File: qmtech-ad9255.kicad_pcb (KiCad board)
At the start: 4 copper layers, 50 x 80 mm, 49 parts

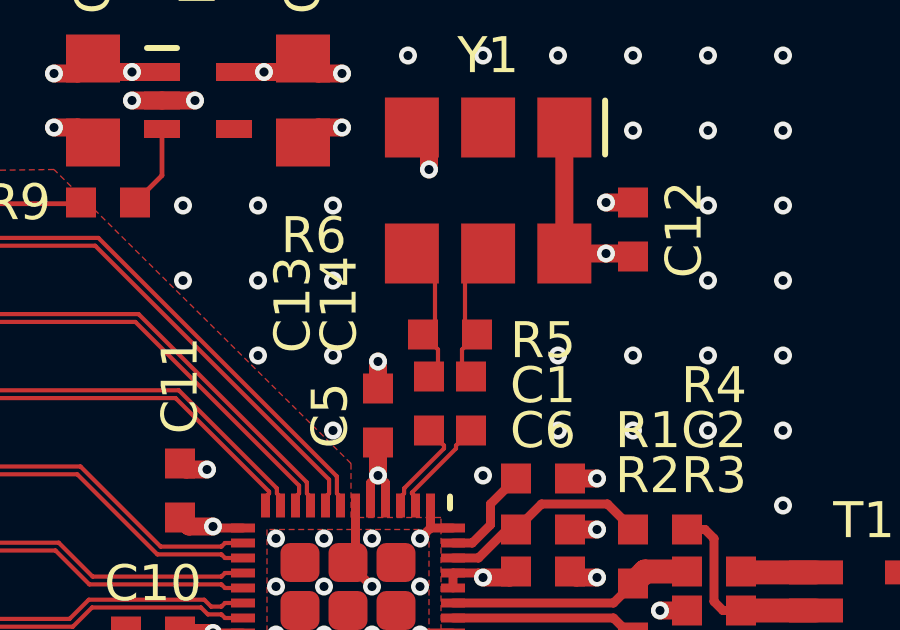
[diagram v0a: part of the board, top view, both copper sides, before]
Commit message: set width of clock traces to 0.3 in qmtech-ad9255
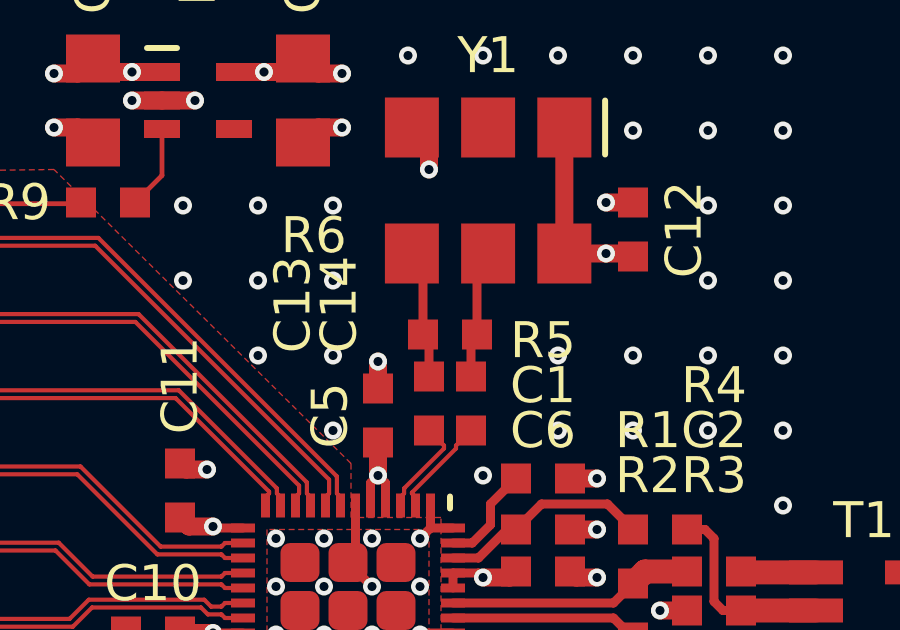
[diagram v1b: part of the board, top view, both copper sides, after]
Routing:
- net CLK-: track 4.92 -> 4.34 mm
- net CLK+: track 4.92 -> 4.34 mm
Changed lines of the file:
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@@
   (segment (start 150.2 97.17) (end 150.2 97.45) (width 0.14) (layer "F.Cu") (net 38))
   (segment (start 150.2 97.45) (end 150.25 97.5) (width 0.14) (layer "F.Cu") (net 38))
-  (segment (start 150.9 89.87) (end 150.13 89.1) (width 0.14) (layer "F.Cu") (net 39))
-  (segment (start 150.5 91.8) (end 150.9 91.4) (width 0.14) (layer "F.Cu") (net 39))
-  (segment (start 150.9 91.4) (end 150.9 89.87) (width 0.14) (layer "F.Cu") (net 39))
-  (segment (start 151 92.9) (end 150.7 93.2) (width 0.14) (layer "F.Cu") (net 39))
-  (segment (start 151 92.3) (end 151 92.9) (width 0.14) (layer "F.Cu") (net 39))
-  (segment (start 150.5 91.8) (end 151 92.3) (width 0.14) (layer "F.Cu") (net 39))
-  (segment (start 152.3 91.8) (end 151.9 91.4) (width 0.14) (layer "F.Cu") (net 40))
-  (segment (start 151.9 91.4) (end 151.9 89.87) (width 0.14) (layer "F.Cu") (net 40))
-  (segment (start 152.3 91.8) (end 151.8 92.3) (width 0.14) (layer "F.Cu") (net 40))
-  (segment (start 151.8 92.9) (end 152.1 93.2) (width 0.14) (layer "F.Cu") (net 40))
-  (segment (start 151.8 92.3) (end 151.8 92.9) (width 0.14) (layer "F.Cu") (net 40))
-  (segment (start 151.9 89.87) (end 152.67 89.1) (width 0.14) (layer "F.Cu") (net 40))
+  (segment (start 150.7 92) (end 150.5 91.8) (width 0.3) (layer "F.Cu") (net 39))
+  (segment (start 150.5 89.47) (end 150.13 89.1) (width 0.3) (layer "F.Cu") (net 39))
+  (segment (start 150.5 91.8) (end 150.5 89.47) (width 0.3) (layer "F.Cu") (net 39))
+  (segment (start 150.7 93.2) (end 150.7 92) (width 0.3) (layer "F.Cu") (net 39))
+  (segment (start 152.1 93.2) (end 152.1 92) (width 0.3) (layer "F.Cu") (net 40))
+  (segment (start 152.1 92) (end 152.3 91.8) (width 0.3) (layer "F.Cu") (net 40))
+  (segment (start 152.3 89.47) (end 152.67 89.1) (width 0.3) (layer "F.Cu") (net 40))
+  (segment (start 152.3 91.8) (end 152.3 89.47) (width 0.3) (layer "F.Cu") (net 40))
   (segment (start 138.2 124.1) (end 139 124.1) (width 0.6) (layer "F.Cu") (net 41))
   (segment (start 139 124.1) (end 139.5 123.6) (width 0.6) (layer "F.Cu") (net 41))

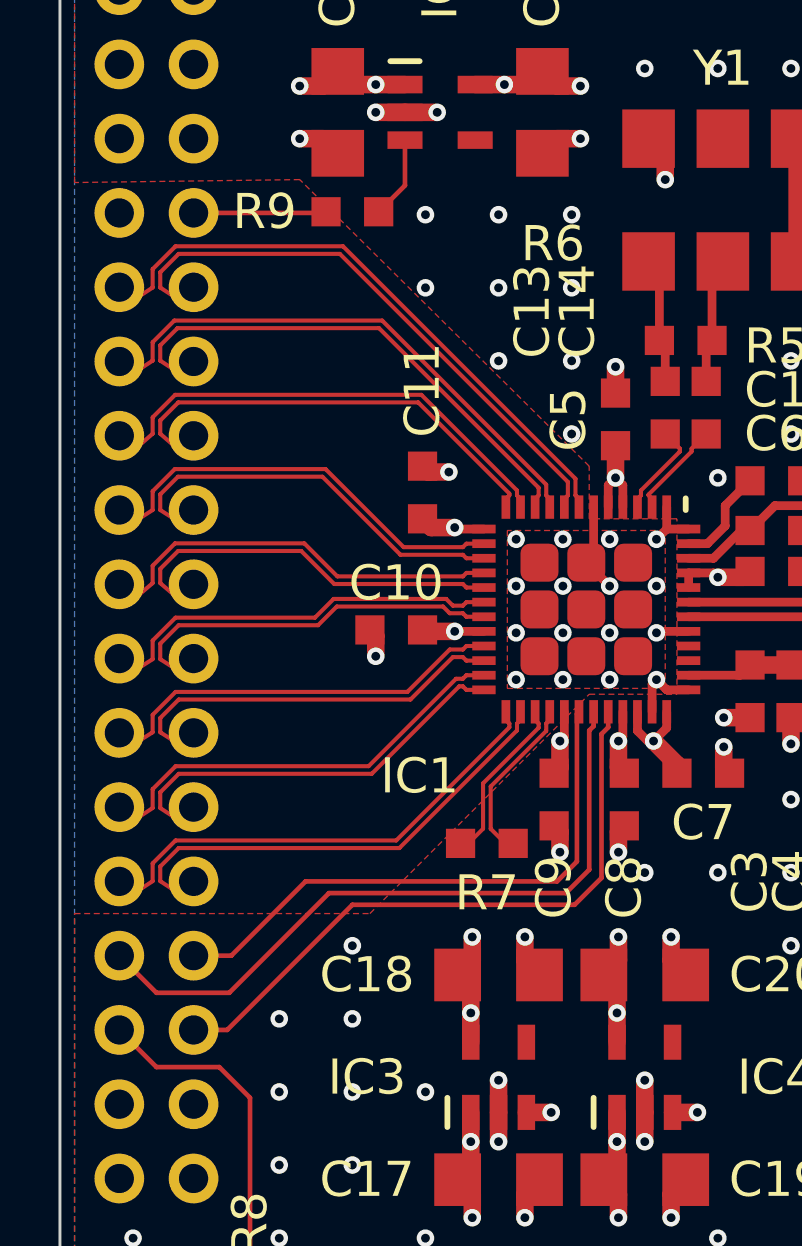
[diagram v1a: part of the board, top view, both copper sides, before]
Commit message: add resistors to SPI inputs in qmtech-ad9255
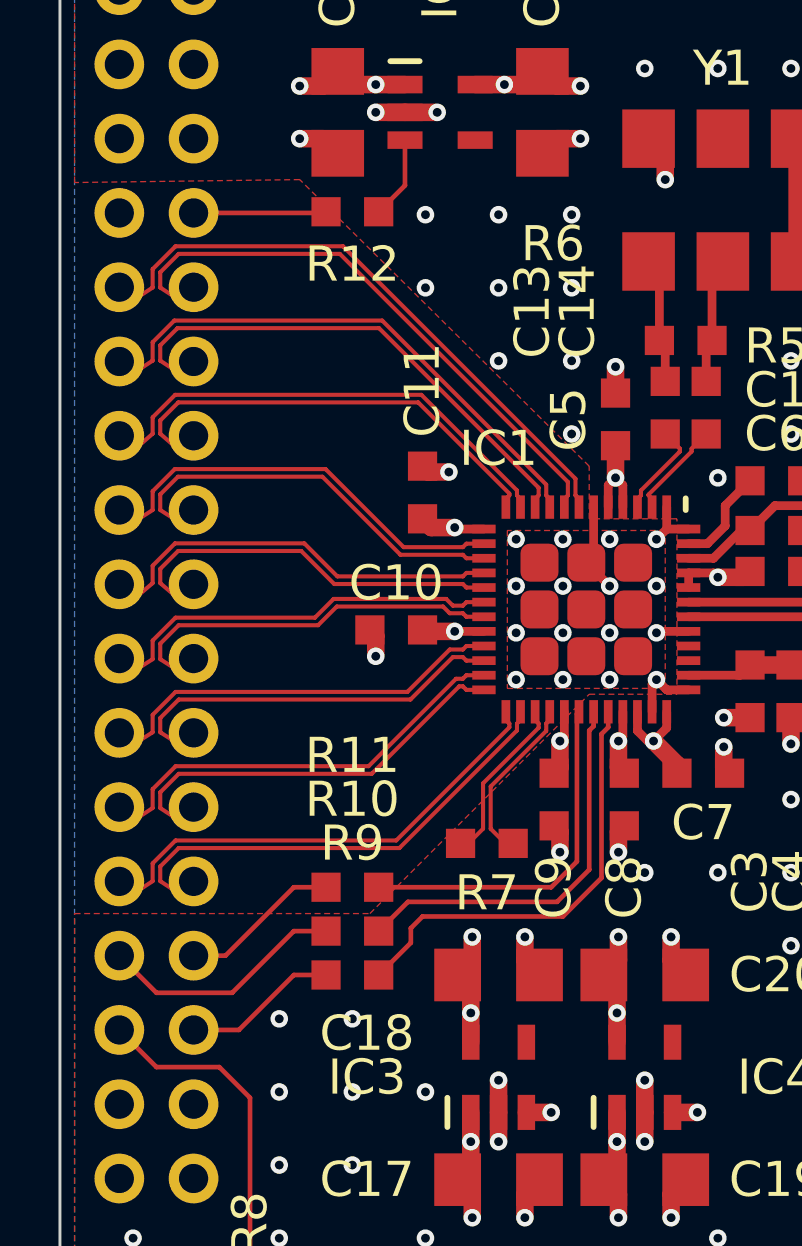
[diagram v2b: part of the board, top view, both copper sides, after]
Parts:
- added R10: , footprints:0603, F.Cu at (140.0, 112.0)
- added R11: , footprints:0603, F.Cu at (140.0, 110.5)
- added R9: , footprints:0603, F.Cu at (140.0, 113.5)
- renumbered R9 to R12
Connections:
- CN2 pad 24: IN2 -> IN5
- CN2 pad 43: SCLK -> IN3
- CN2 pad 44: SDIO -> IN4
- CN2 pad 46: CSB -> IN2
- R12 pad 1: IN2 -> IN5
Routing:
- net SCLK: track 23.8 -> 13.5 mm
- net IN3: track 0.00 -> 8.47 mm
- net SDIO: track 19.6 -> 12.3 mm
- net CSB: track 21.9 -> 15.1 mm
- net IN4: track 0.00 -> 5.50 mm
- net IN5: track 0.00 -> 4.55 mm
- net IN2: track 4.55 -> 5.31 mm
- net GND: vias 190 -> 189

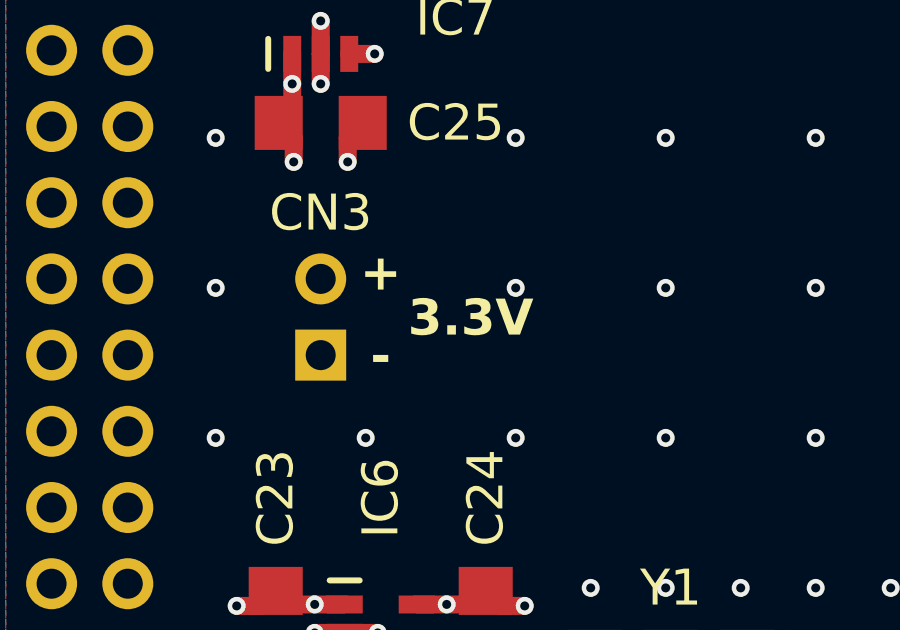
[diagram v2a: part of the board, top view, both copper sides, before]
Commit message: improve CN3 pin designation
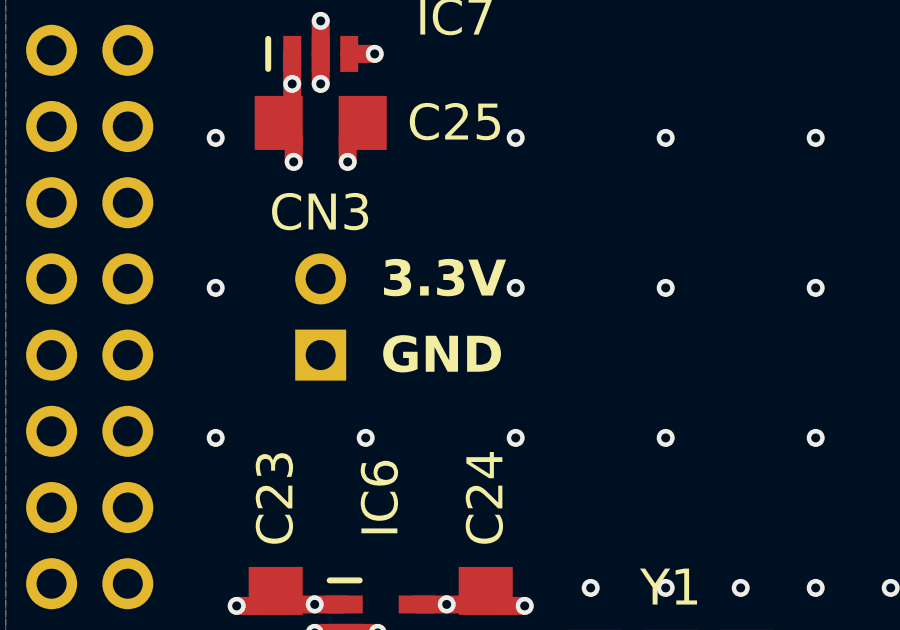
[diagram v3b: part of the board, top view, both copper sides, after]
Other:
- board text added: "GND"
- board text removed: "+"
- board text removed: "-"
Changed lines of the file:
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@@
   (gr_rect (start 130 50) (end 180 130)
     (stroke (width 0.1) (type solid)) (fill none) (layer "Edge.Cuts"))
-  (gr_text "+" (at 143 72) (layer "F.SilkS")
-    (effects (font (size 1.2 1.2) (thickness 0.2) bold))
+  (gr_text "GND" (at 143 74.74) (layer "F.SilkS")
+    (effects (font (size 1.2 1.2) (thickness 0.2) bold) (justify left))
   )
-  (gr_text "-" (at 143 74.77) (layer "F.SilkS")
-    (effects (font (size 1.2 1.2) (thickness 0.2) bold))
-  )
-  (gr_text "3.3V" (at 146 73.5) (layer "F.SilkS")
-    (effects (font (size 1.2 1.2) (thickness 0.2) bold))
+  (gr_text "3.3V" (at 143 72.2) (layer "F.SilkS")
+    (effects (font (size 1.2 1.2) (thickness 0.2) bold) (justify left))
   )
   (segment (start 149.25 97.5) (end 149.25 96.75) (width 0.3) (layer "F.Cu") (net 1))

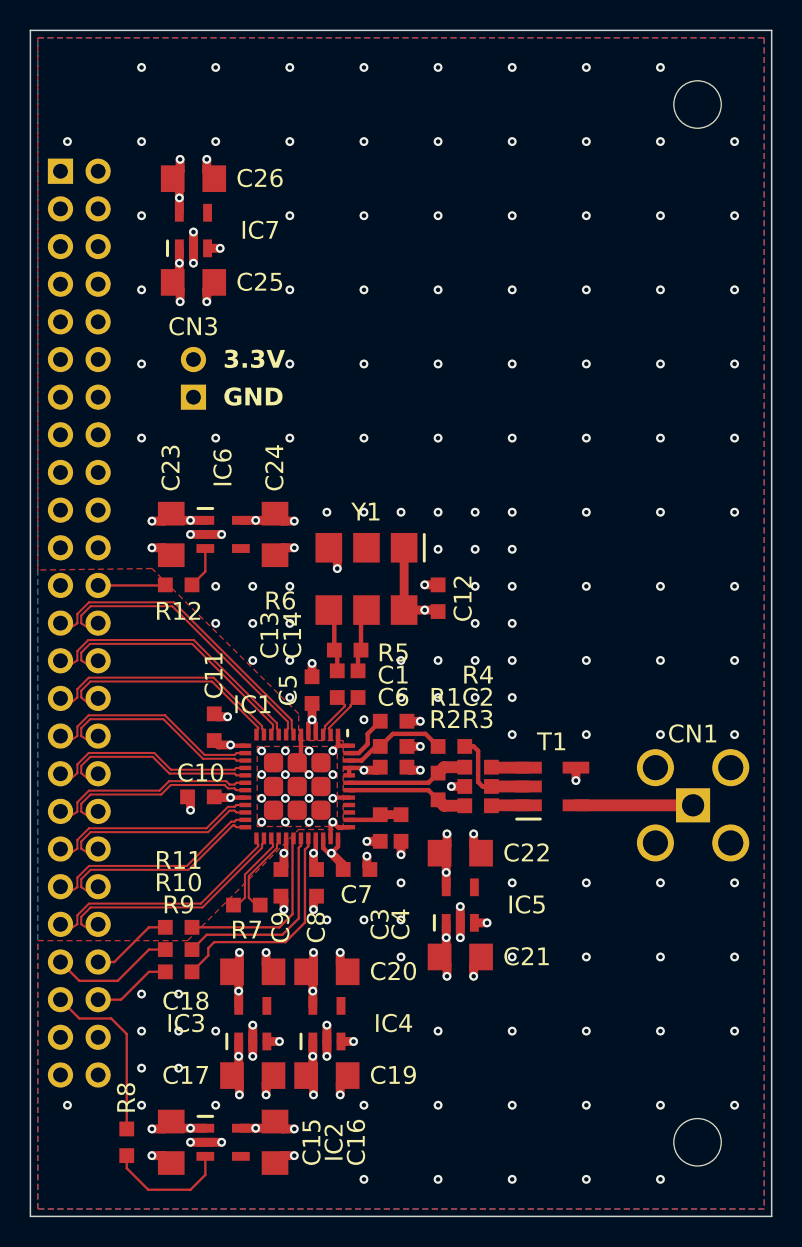
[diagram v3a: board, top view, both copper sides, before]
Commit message: replace SMA through-hole connector with SMA edge connector in qmtech-ad9255
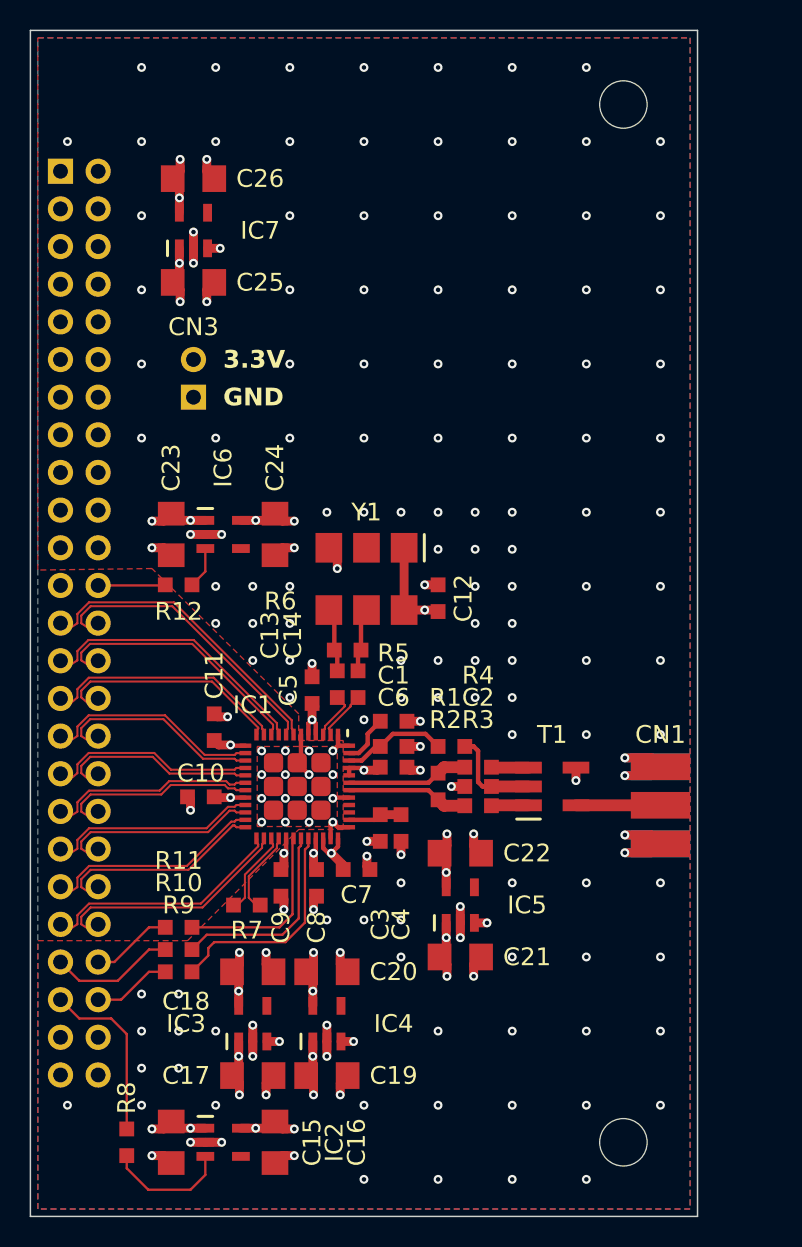
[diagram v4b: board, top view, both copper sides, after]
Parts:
- CN1: footprint footprints:SMA -> footprints:SMA-EDGE
- moved M1 5.00 mm to (170.0, 125.0)
- moved M2 5.00 mm to (170.0, 55.0)
- moved CN1 2.20 mm to (172.5, 102.3), turned to -90 degrees
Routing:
- net GND: track 53.8 -> 75.0 mm, vias 189 -> 178
- net INPUT: track 7.90 -> 5.70 mm
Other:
- board size 50 x 80 mm -> 45 x 80 mm
